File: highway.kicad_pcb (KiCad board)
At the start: 2 copper layers, 7 parts, among them SW1 SW_Push, SW2 SW_Push, SW3 SW_Push, SW4 SW_Push, U1 XIAO-RP2040-DIP

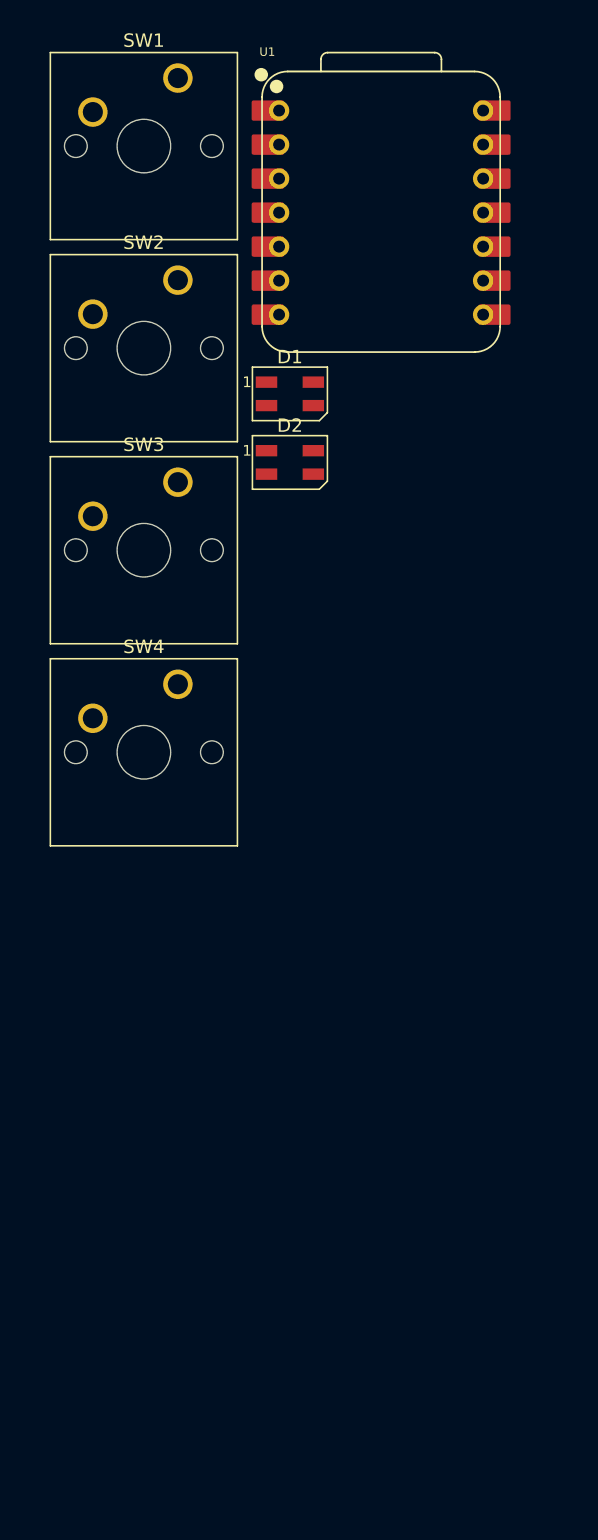
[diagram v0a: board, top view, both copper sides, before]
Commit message: add new case
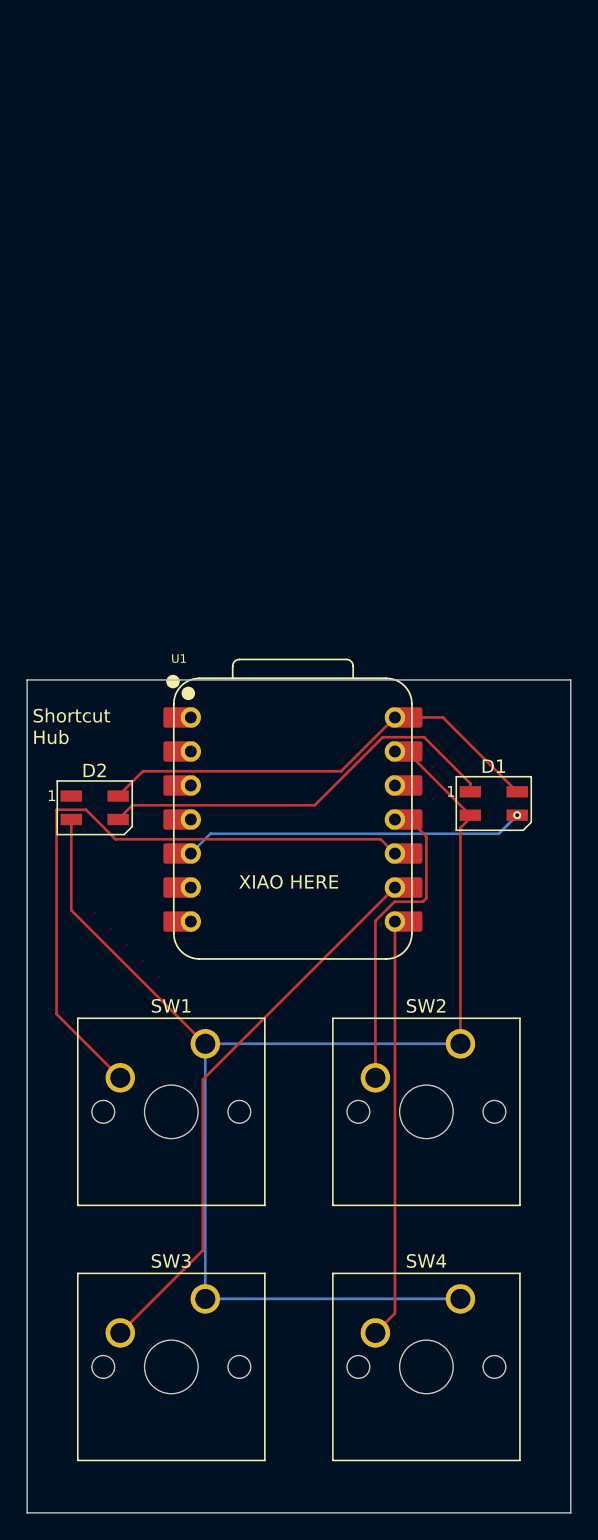
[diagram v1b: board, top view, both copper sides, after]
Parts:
- moved SW1 72.1 mm to (133.5, 128.3)
- moved SW3 61.0 mm to (133.5, 147.3)
- moved SW2 60.8 mm to (152.6, 128.3)
- moved SW4 50.5 mm to (152.6, 147.3)
- moved U1 45.8 mm to (140.0, 111.5)
- moved D1 34.2 mm to (155.1, 110.3)
- moved D2 29.6 mm to (125.2, 110.6)
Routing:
- net GND: track 0.00 -> 103.2 mm
- net Net-(U1-GPIO4/MISO): track 0.00 -> 48.6 mm
- net Net-(U1-GPIO2/SCK): track 0.00 -> 41.8 mm
- net +5V: track 0.00 -> 34.5 mm
- net Net-(U1-GPIO1/RX): track 0.00 -> 31.3 mm
- net Net-(D1-VSS): track 0.00 -> 30.9 mm
- net Net-(D1-VDD): track 0.00 -> 25.6 mm, vias 0 -> 1
- net Net-(U1-GPIO3/MOSI): track 0.00 -> 23.7 mm
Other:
- board outline added: 40.6 x 62.2 mm
- board text added: "Shortcut Hub"
- board text added: "XIAO HERE"
